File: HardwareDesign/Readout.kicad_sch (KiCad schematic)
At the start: 4 parts, among them U2 74ACT163, U3 74ACT163, U4 74ACT163, U5 74ACT163

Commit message: working on Readout module
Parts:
- added U705, U706: 74ACT273, symbol 74xx:74LS273
- renumbered U2 to U701, U3 to U702, U4 to U703, U5 to U704
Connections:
- net GND: now also U701.8 (GND), U702.8 (GND), U703.8 (GND), U704.8 (GND), U705.10 (GND), U706.10 (GND), U706.14 (D5), U706.17 (D6), U706.18 (D7)
- net RowBeginA0: now also U705.2 (Q0)
- net RowBeginA1: now also U705.5 (Q1)
- net RowBeginA10: now also U706.6 (Q2)
- net RowBeginA11: now also U706.9 (Q3)
- net RowBeginA12: now also U706.12 (Q4)
- net RowBeginA2: now also U705.6 (Q2)
- net RowBeginA3: now also U705.9 (Q3)
- net RowBeginA4: now also U705.12 (Q4)
- net RowBeginA5: now also U705.15 (Q5)
- net RowBeginA6: now also U705.16 (Q6)
- net RowBeginA7: now also U705.19 (Q7)
- net RowBeginA8: now also U706.2 (Q0)
- net RowBeginA9: now also U706.5 (Q1)
- net ReadoutA7: now reaches U702.11 (Q3)
- net ReadoutA7: now also U705.18 (D7)
- net ReadoutA6: now reaches U702.12 (Q2)
- net ReadoutA6: now also U705.17 (D6)
- net ReadoutA5: now reaches U702.13 (Q1)
- net ReadoutA5: now also U705.14 (D5)
- net ReadoutA4: now reaches U702.14 (Q0)
- net ReadoutA4: now also U705.13 (D4)
- net VCC: now reaches U702.16 (VCC)
- net VCC: now also U701.16 (VCC), U703.16 (VCC), U704.16 (VCC), U705.20 (VCC), U706.20 (VCC)
- net ReadoutA11: now reaches U703.11 (Q3)
- net ReadoutA11: now also U706.8 (D3)
- net ReadoutA10: now reaches U703.12 (Q2)
- net ReadoutA10: now also U706.7 (D2)
- net ReadoutA9: now reaches U703.13 (Q1)
- net ReadoutA9: now also U706.4 (D1)
- net ReadoutA8: now reaches U703.14 (Q0)
- net ReadoutA8: now also U706.3 (D0)
- net ReadoutA3: now reaches U701.11 (Q3)
- net ReadoutA3: now also U705.8 (D3)
- net ReadoutA2: now reaches U701.12 (Q2)
- net ReadoutA2: now also U705.7 (D2)
- net ReadoutA1: now reaches U701.13 (Q1)
- net ReadoutA1: now also U705.4 (D1)
- net ReadoutA0: now reaches U701.14 (Q0)
- net ReadoutA0: now also U705.3 (D0)
- net ReadoutA12: now reaches U704.14 (Q0)
- net ReadoutA12: now also U706.13 (D4)
- new net RowBeginA13: U706.15 (Q5)
- new net RowBeginA14: U706.16 (Q6)
- new net RowBeginA15: U706.19 (Q7)
- no-connect marks 0 -> 4
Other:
- note added: "Readout address register"
- note added: "Row begin address register"
- moved on the sheet: U702, U703, U704

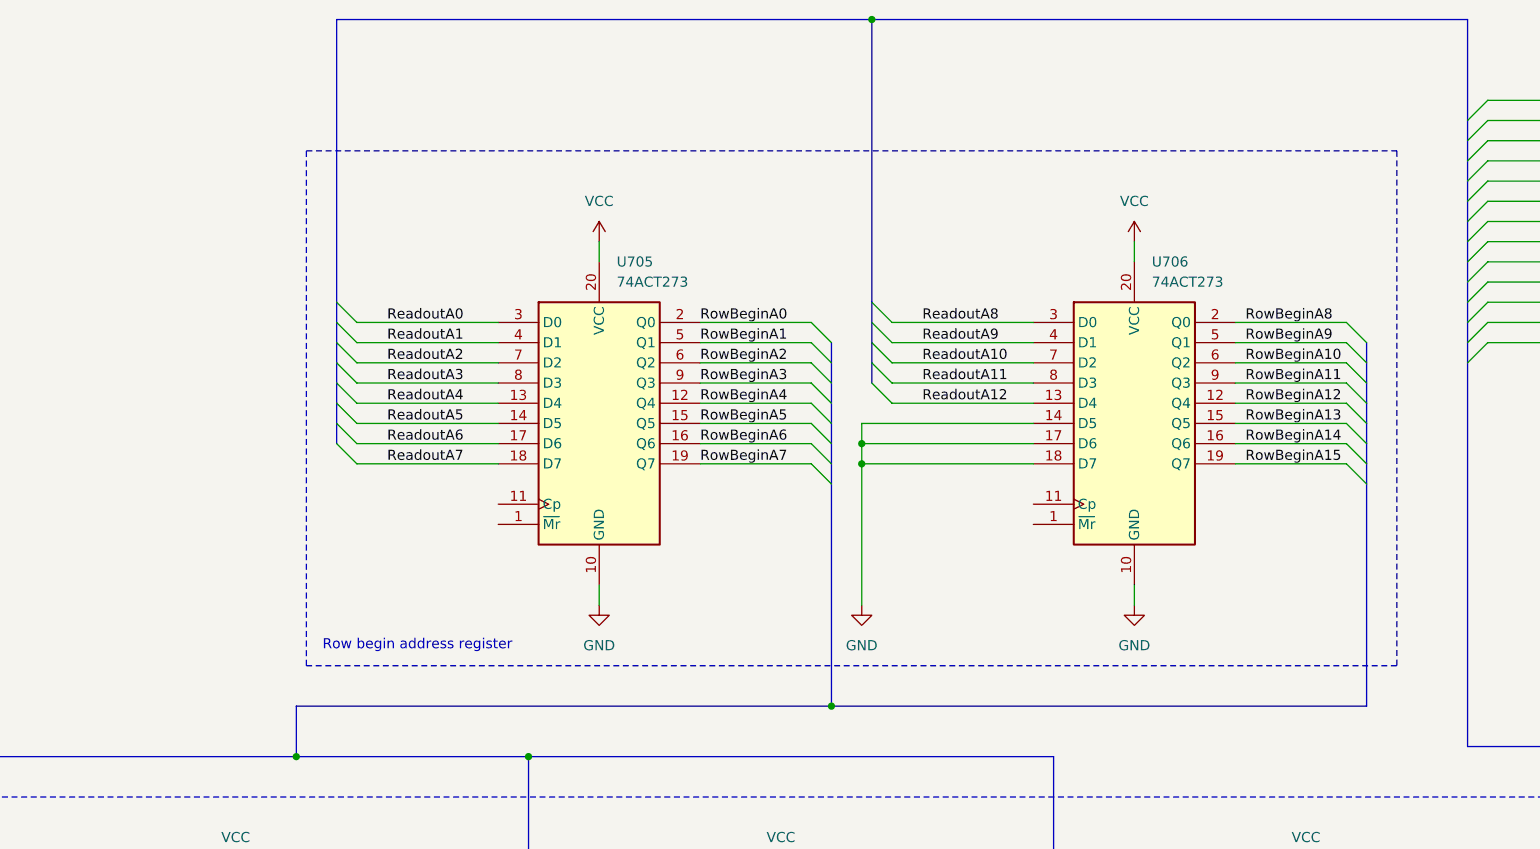
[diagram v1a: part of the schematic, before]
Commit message: use -VSYNC to clear row begin address register
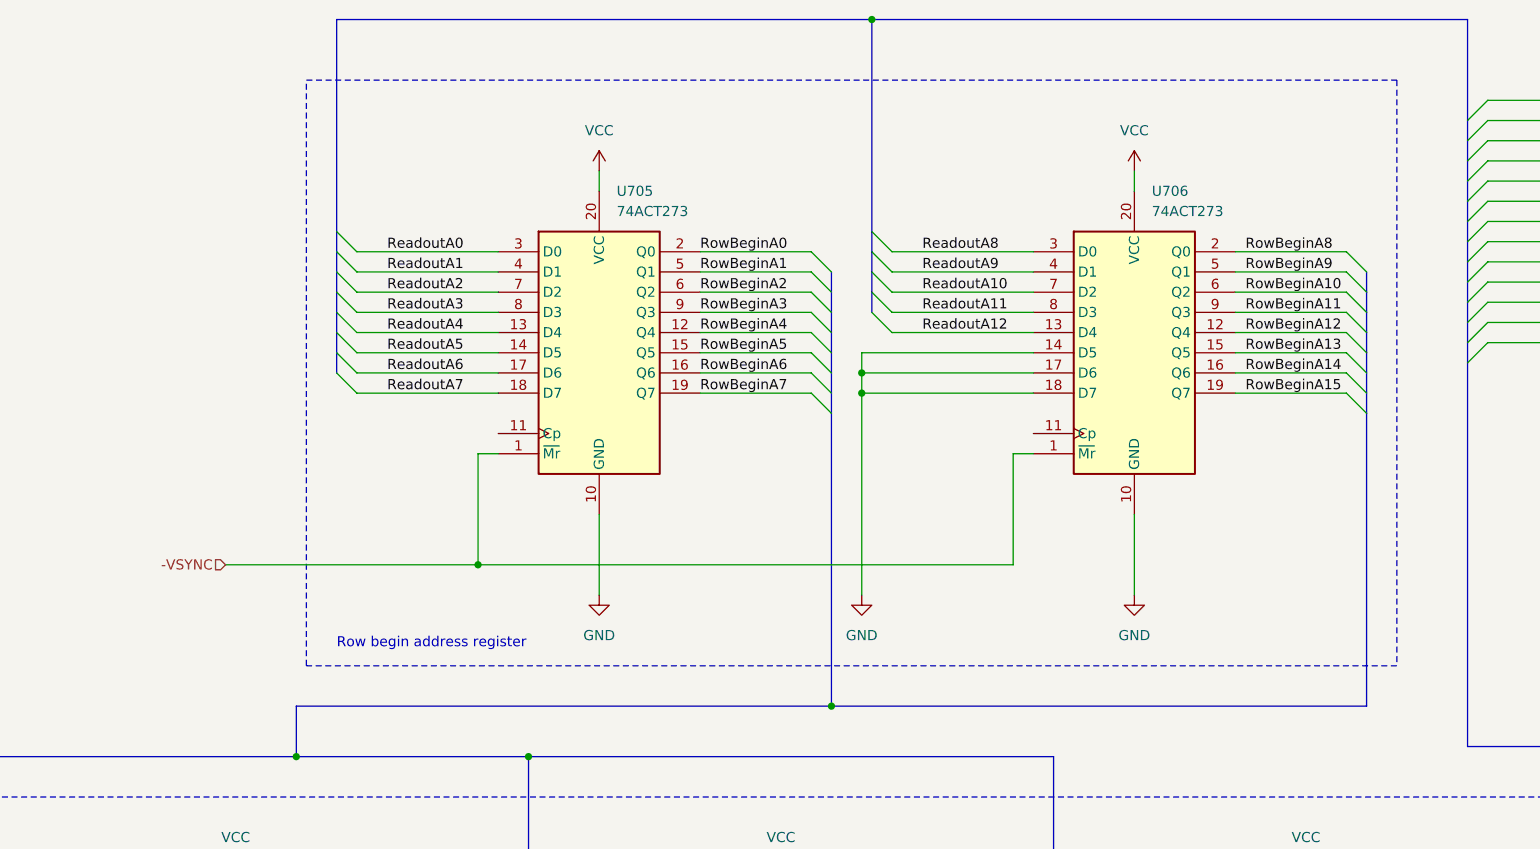
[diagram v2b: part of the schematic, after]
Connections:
- net -VSYNC: now reaches U706.1 (~{Mr})
- net -VSYNC: now also U705.1 (~{Mr})
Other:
- moved on the sheet: U705, U706

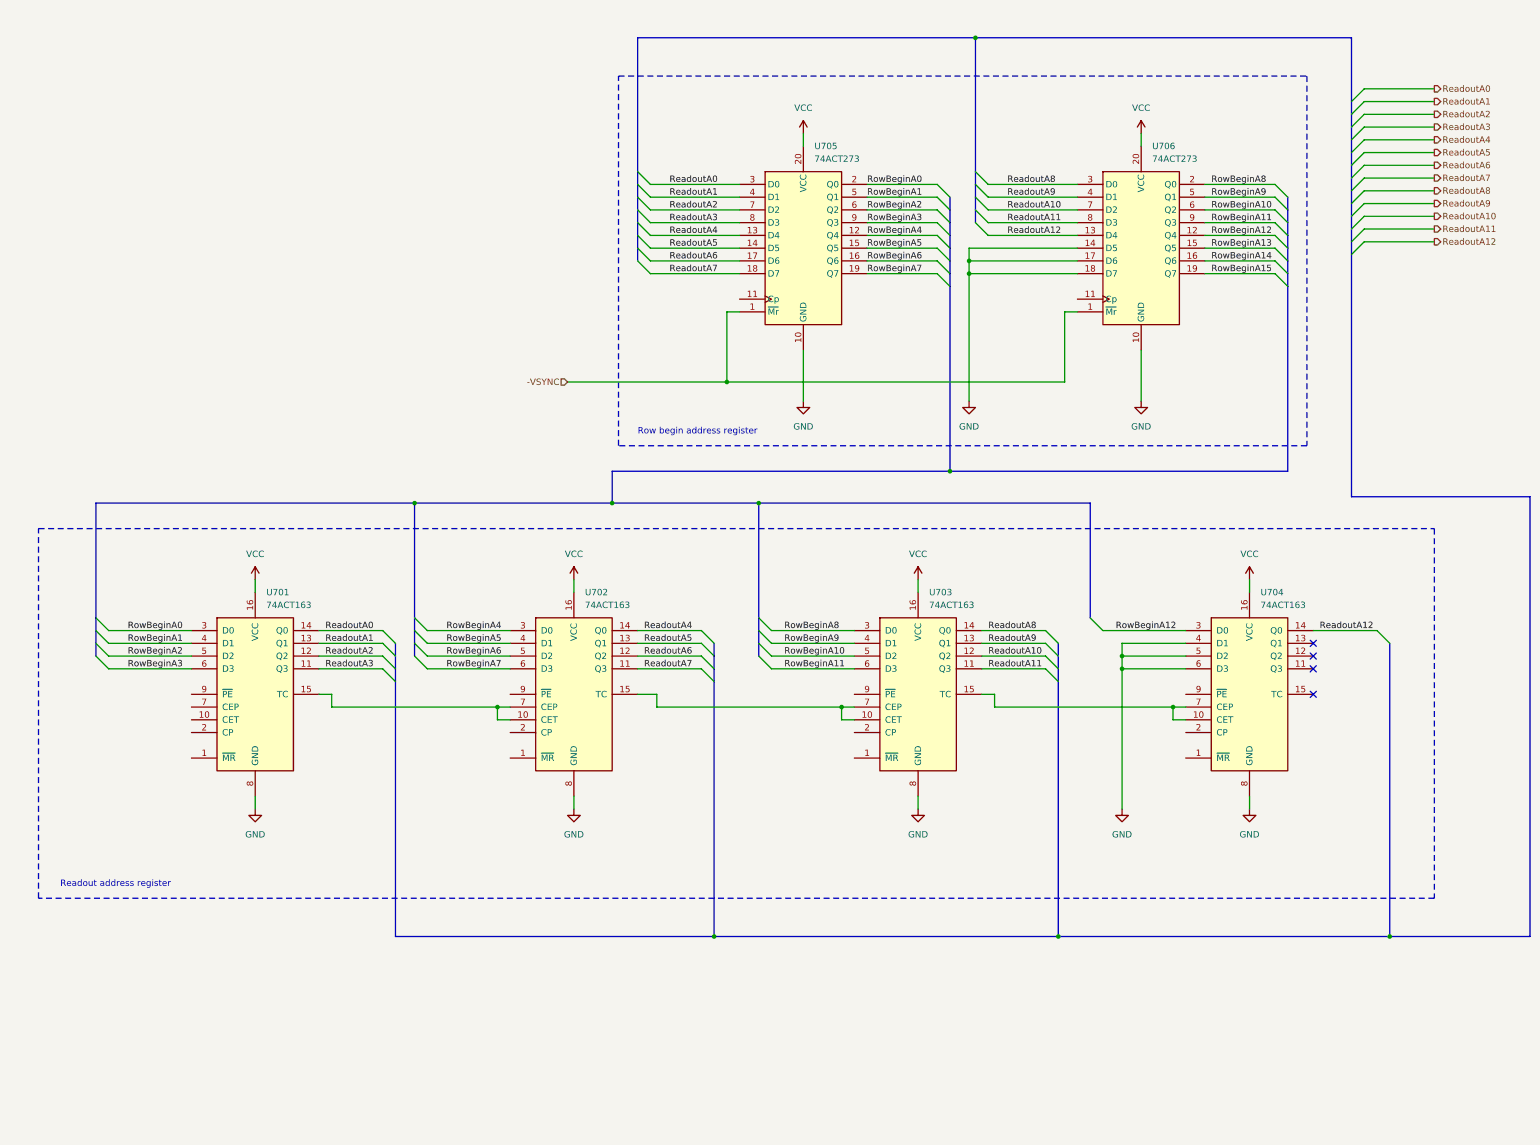
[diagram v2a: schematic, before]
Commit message: more work on Readout module
Eliminate the 4th 74ACT163 counter managing ReadoutA12:
we should be able to replace it with a single flip-flop
in the Readout control GAL.

Started working on control signals.
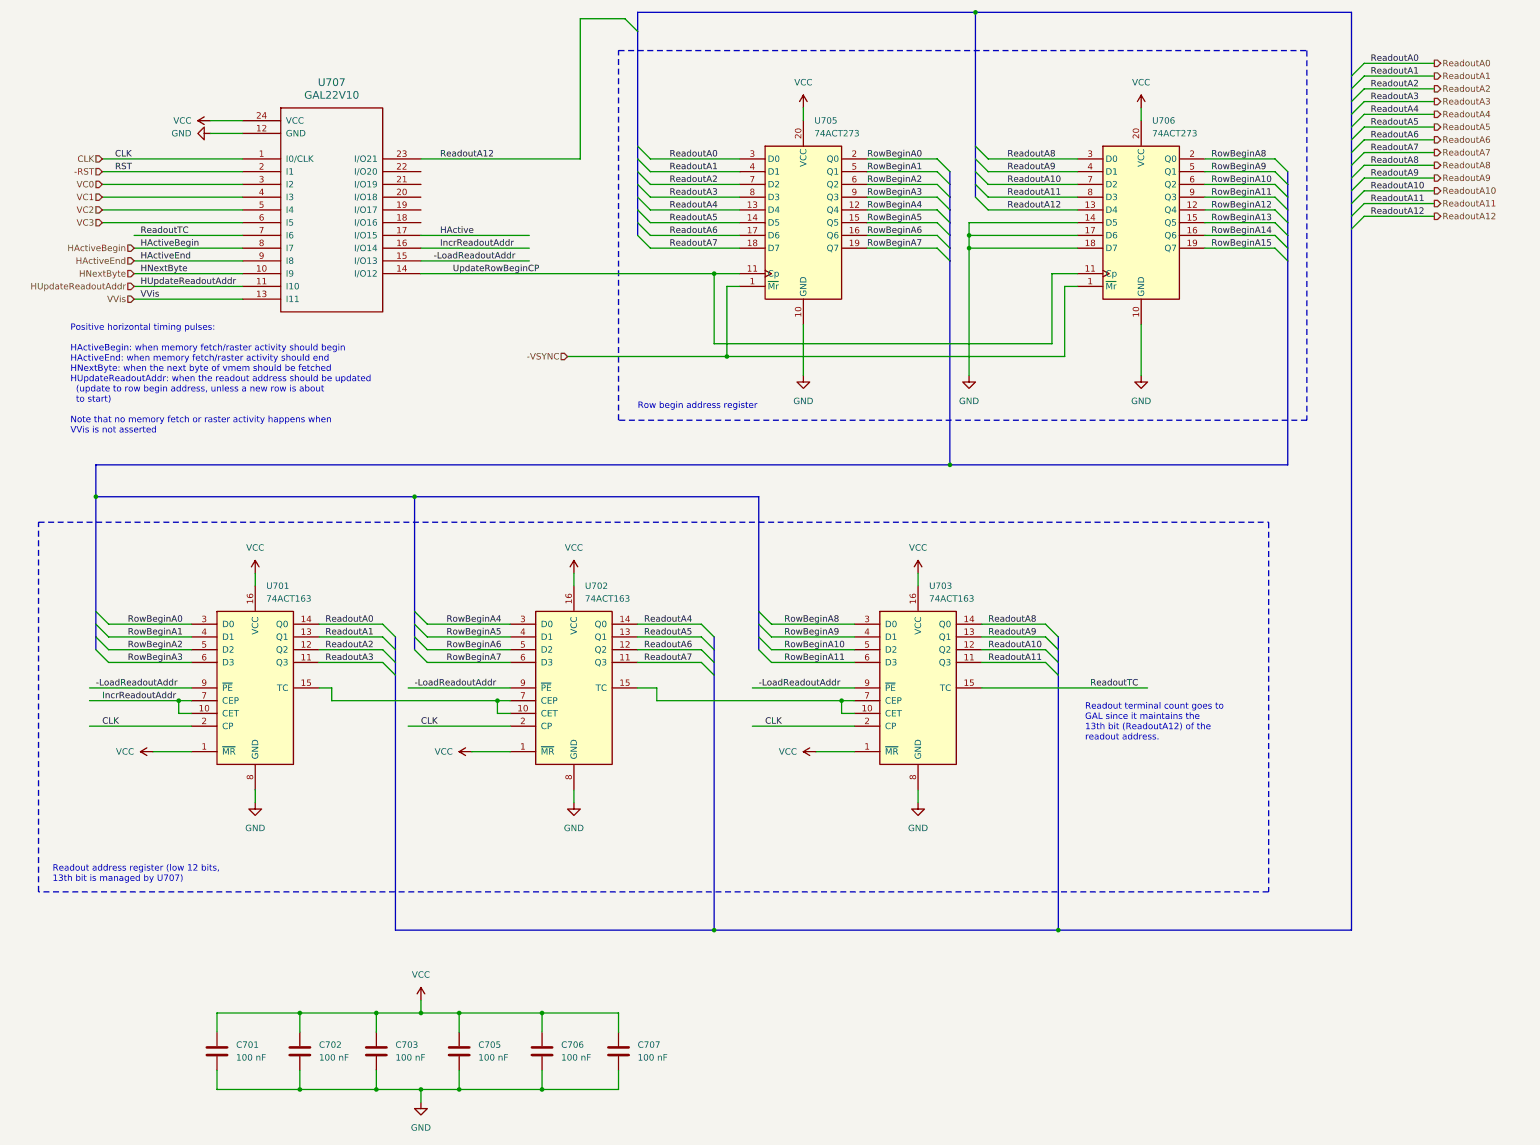
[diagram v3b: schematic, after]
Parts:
- removed U704: 74ACT163, symbol 74xx:74LS163
- added C701, C702, C703, C705, C706, C707: 100 nF, symbol Device:C
- added U707: GAL22V10, symbol ya68k:GAL22V10
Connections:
- net GND: now also C701.2, C702.2, C703.2, C705.2, C706.2, C707.2, U707.12 (GND)
- net ReadoutA12: now also U707.23 (I/O21)
- net VCC: now also U701.1 (~{MR}), U702.1 (~{MR}), U703.1 (~{MR}), C701.1, C702.1, C703.1, C705.1, C706.1, C707.1, U707.24 (VCC)
- net CLK: now reaches U702.2 (CP)
- net CLK: now also U701.2 (CP), U703.2 (CP), U707.1 (I0/CLK)
- net -LoadReadoutAddr: now reaches U702.9 (~{PE})
- net -LoadReadoutAddr: now also U701.9 (~{PE}), U703.9 (~{PE}), U707.15 (I/O13)
- net ReadoutTC: now reaches U703.15 (TC)
- net ReadoutTC: now also U707.7 (I6)
- net UpdateRowBeginCP: now reaches U706.11 (Cp)
- net UpdateRowBeginCP: now also U705.11 (Cp), U707.14 (I/O12)
- net IncrReadoutAddr: now reaches U701.10 (CET)
- net IncrReadoutAddr: now also U701.7 (CEP), U707.16 (I/O14)
- new net -RST: U707.2 (I1)
- new net HActive: U707.17 (I/O15)
- new net HActiveBegin: U707.8 (I7)
- new net HActiveEnd: U707.9 (I8)
- new net HNextByte: U707.10 (I9)
- new net HUpdateReadoutAddr: U707.11 (I10)
- new net VC0: U707.3 (I2)
- new net VC1: U707.4 (I3)
- new net VC2: U707.5 (I4)
- new net VC3: U707.6 (I5)
- new net VVis: U707.13 (I11)
- no-connect marks 4 -> 0
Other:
- note added: "Positive horizontal timing pulses: HActiveBegin: when memory fetch/raster activity should begin HActiveEnd: when memory fetch/raster activity should end HNextByte: when the next byte of vmem should be fetched HUpdateReadoutAddr: when the readout address should be updated (update to row begin address, unless a new row is about to start) Note that no memory fetch or raster activity happens when VVi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"
- note added: "Readout address register (low 12 bits, 13th bit is managed by U707)"
- note added: "Readout terminal count goes to GAL since it maintains the 13th bit (ReadoutA12) of the readout address."
- note removed: "Readout address register"
- moved on the sheet: U701, U702, U703, U705, U706

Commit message: update readout schematic with changes from sim
The simulation seems to be working, so in theory this
should be a good hardware design.
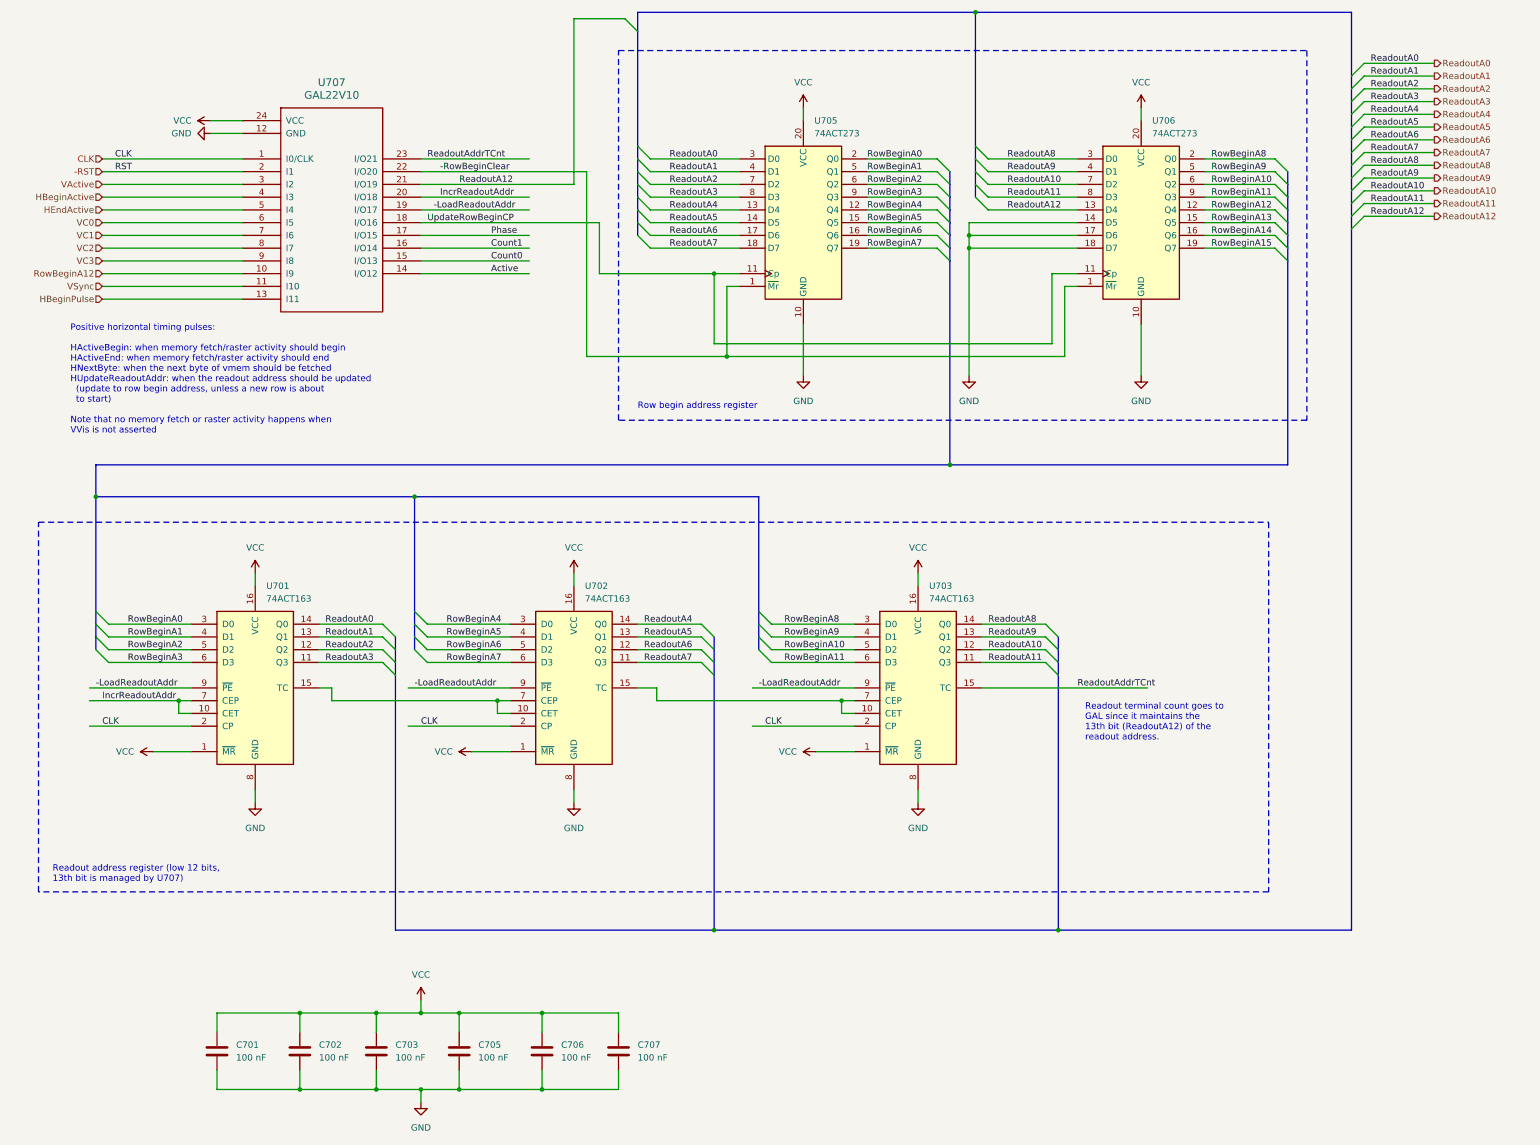
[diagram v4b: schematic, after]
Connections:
- net -VSYNC is gone; now on net -RowBeginClear: U705.1 (~{Mr}), U706.1 (~{Mr})
- net HActiveBegin is gone; now on net VC2: U707.8 (I7)
- net HActiveEnd is gone; now on net VC3: U707.9 (I8)
- net HNextByte is gone; now on net RowBeginA12: U707.10 (I9)
- net -LoadReadoutAddr: now also U707.19 (I/O17); no longer U707.15 (I/O13)
- net IncrReadoutAddr: now also U707.20 (I/O18); no longer U707.16 (I/O14)
- net ReadoutA12: now also U707.21 (I/O19); no longer U707.23 (I/O21)
- net UpdateRowBeginCP: now also U707.18 (I/O16); no longer U707.14 (I/O12)
- net VC0: now also U707.6 (I5); no longer U707.3 (I2)
- net VC1: now also U707.7 (I6); no longer U707.4 (I3)
- net VC2: no longer U707.5 (I4)
- net VC3: no longer U707.6 (I5)
- net -RowBeginClear: now reaches U707.22 (I/O20)
- net HActive renamed Phase
- net HUpdateReadoutAddr renamed VSync
- net ReadoutTC renamed ReadoutAddrTCnt
- net ReadoutAddrTCnt: now also U707.23 (I/O21); no longer U707.7 (I6)
- net VVis renamed HBeginPulse
- new net Active: U707.14 (I/O12)
- new net Count0: U707.15 (I/O13)
- new net Count1: U707.16 (I/O14)
- new net HBeginActive: U707.4 (I3)
- new net HEndActive: U707.5 (I4)
- new net VActive: U707.3 (I2)

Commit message: more main sheet cleanups
Also removed one unneeded pin (ReadoutA12) for the
Readout module: it's a purely internal signal.
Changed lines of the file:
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@@
+		)
+	)
+	(label "RowBeginA12"
+		(at 35.56 67.31 0)
+		(fields_autoplaced yes)
+		(effects
+			(font
+				(size 1.27 1.27)
+			)
+			(justify left bottom)
 		)
 	)
@@
 		)
 	)
-	(hierarchical_label "RowBeginA12"
-		(shape input)
-		(at 33.02 67.31 180)
-		(fields_autoplaced yes)
-		(effects
-			(font
-				(size 1.27 1.27)
-			)
-			(justify right)
-		)
-	)
